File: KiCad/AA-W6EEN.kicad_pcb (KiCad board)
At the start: 2 copper layers, 90 x 44 mm, 68 parts, among them J1 ANT, J2 BATT-MODULE, J3 2.4" TFT with EC11, Q1 BF998, Q2 AO3401A, Q3 MMBT2222A, T1 Bifilar-10T, U1 Si5351A-B-GT, U2 LM358, U3 AMS1117-3.3

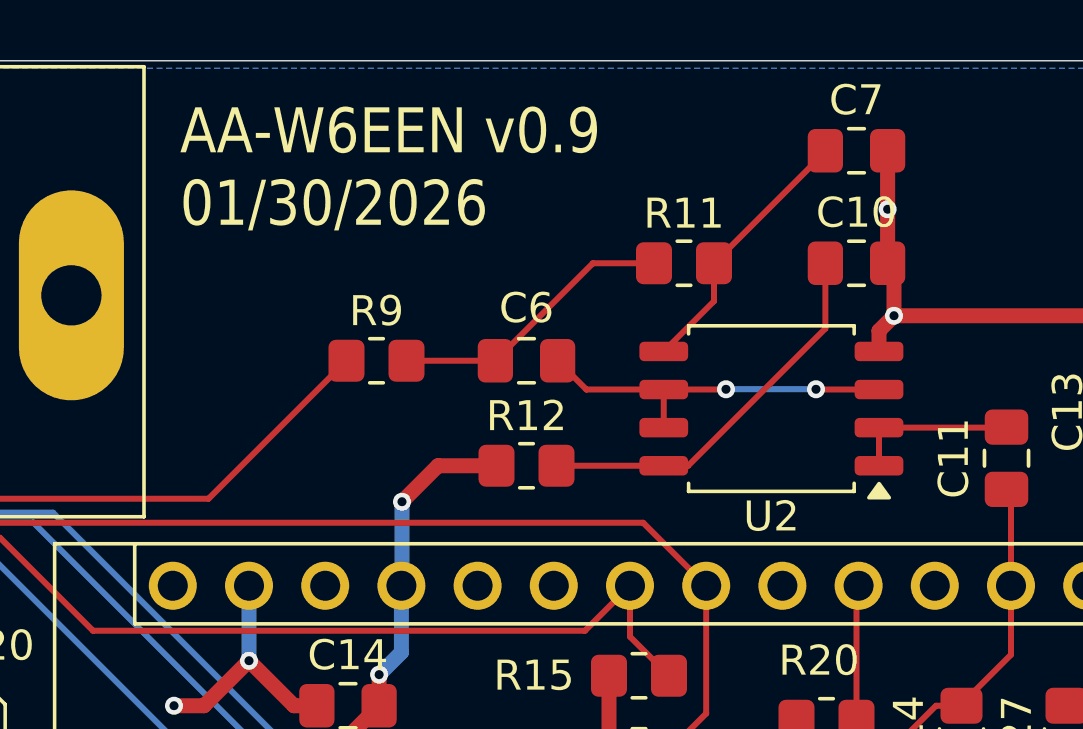
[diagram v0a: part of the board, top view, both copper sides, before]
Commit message: Updated OPAMP footprint. Changed date/revision.
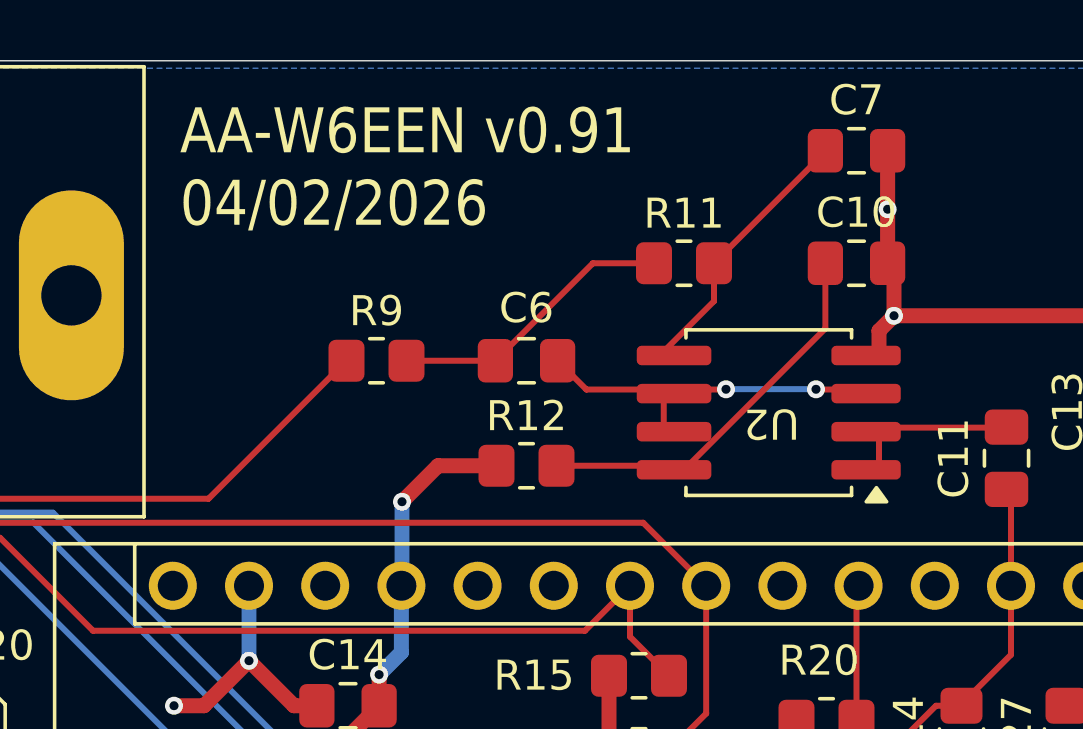
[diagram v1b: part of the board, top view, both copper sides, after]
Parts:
- U2: footprint Package_SO:SOIC-8_5.3x5.3mm_P1.27mm -> MY-SOIC8:My-SOIC8
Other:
- board text added: "AA-W6EEN v0.91 04/02/2026"
- board text removed: "AA-W6EEN v0.9 01/30/2026"
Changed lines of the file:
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@@
 		)
 	)
-	(footprint "Package_SO:SOIC-8_5.3x5.3mm_P1.27mm"
+	(footprint "MY-SOIC8:My-SOIC8"
 		(layer "F.Cu")
 		(at 100.4125 51.595 180)
-		(descr "SOIC, 8 Pin (JEITA/EIAJ ED-7311-19 variation 08-001-BBA and Atmel/Microchip, 208 mils width, https://www.jeita.or.jp/japanese/standard/book/ED-7311-19/#target/page_no=21, https://ww1.microchip.com/downloads/en/DeviceDoc/20005045C.pdf#page=23, https://ww1.microchip.com/downloads/en/DeviceDoc/doc2535.pdf#page=162), generated with kicad-footprint-generator ipc_gullwing_generator.py")
-		(tags "SOIC SO P-SOP SOP SOP-8 SO SO-8 8S2 S2AE/F K04-056 CASE-751BE SO8W 8-Pin-SOIC PSA W8-2 W8-4 W8MS-1 FPT-8P-M08")
 		(property "Reference" "U2"
-			(at 0 -3.6 0)
+			(at 0 -0.5 180)
+			(unlocked yes)
 			(layer "F.SilkS")
 			(effects
 				(font
 					(size 1 1)
-					(thickness 0.15)
+					(thickness 0.1)
 				)
 			)
 		)
 		(property "Value" "LM358"
-			(at 0 3.6 0)
+			(at 0 1 180)
+			(unlocked yes)
 			(layer "F.Fab")
 			(hide yes)
@@
 		)
 		(property "Datasheet" "http://www.ti.com/lit/ds/symlink/lm2904-n.pdf"
-			(at 0 0 0)
+			(at 0 0 180)
+			(unlocked yes)
 			(layer "F.Fab")
 			(hide yes)
 			(effects
 				(font
-					(size 1.27 1.27)
+					(size 1 1)
 					(thickness 0.15)
 				)
@@
 		)
 		(property "Description" "Low-Power, Dual Operational Amplifiers, DIP-8/SOIC-8/TO-99-8"
-			(at 0 0 0)
+			(at 0 0 180)
+			(unlocked yes)
 			(layer "F.Fab")
 			(hide yes)
 			(effects
 				(font
-					(size 1.27 1.27)
+					(size 1 1)
 					(thickness 0.15)
 				)
@@
 		(attr smd)
 		(fp_line
-			(start 2.76 2.76)
-			(end -2.76 2.76)
+			(start 2.8475 2.625)
+			(end -2.6725 2.625)
 			(stroke
 				(width 0.12)
@@
 		)
 		(fp_line
-			(start 2.76 2.49)
-			(end 2.76 2.76)
+			(start 2.8475 2.355)
+			(end 2.8475 2.625)
 			(stroke
 				(width 0.12)
@@
 		)
 		(fp_line
-			(start 2.76 -2.76)
-			(end 2.76 -2.49)
+			(start 2.8475 -2.895)
+			(end 2.8475 -2.625)
 			(stroke
 				(width 0.12)
@@
 		)
 		(fp_line
-			(start -2.76 2.76)
-			(end -2.76 2.49)
+			(start -2.6725 2.625)
+			(end -2.6725 2.355)
 			(stroke
 				(width 0.12)
@@
 		)
 		(fp_line
-			(start -2.76 -2.49)
-			(end -2.76 -2.76)
+			(start -2.6725 -2.625)
+			(end -2.6725 -2.895)
 			(stroke
 				(width 0.12)
@@
 		)
 		(fp_line
-			(start -2.76 -2.76)
-			(end 2.76 -2.76)
+			(start -2.6725 -2.895)
+			(end 2.8475 -2.895)
 			(stroke
 				(width 0.12)
@@
 		(fp_poly
 			(pts
-				(xy -3.59 -2.5) (xy -3.93 -2.97) (xy -3.25 -2.97)
+				(xy -3.5025 -2.635) (xy -3.8425 -3.105) (xy -3.1625 -3.105)
 			)
 			(stroke
@@
 		)
 		(fp_line
-			(start 4.65 2.48)
-			(end 2.9 2.48)
+			(start 4.7375 2.345)
+			(end 2.9875 2.345)
 			(stroke
 				(width 0.05)
@@
 		)
 		(fp_line
-			(start 4.65 -2.48)
-			(end 4.65 2.48)
+			(start 4.7375 -2.615)
+			(end 4.7375 2.345)
 			(stroke
 				(width 0.05)
@@
 		)
 		(fp_line
-			(start 2.9 2.9)
-			(end -2.9 2.9)
+			(start 2.9875 2.765)
+			(end -2.8125 2.765)
 			(stroke
 				(width 0.05)
@@
 		)
 		(fp_line
-			(start 2.9 2.48)
-			(end 2.9 2.9)
+			(start 2.9875 2.345)
+			(end 2.9875 2.765)
 			(stroke
 				(width 0.05)
@@
 		)
 		(fp_line
-			(start 2.9 -2.48)
-			(end 4.65 -2.48)
+			(start 2.9875 -2.615)
+			(end 4.7375 -2.615)
 			(stroke
 				(width 0.05)
@@
 		)
 		(fp_line
-			(start 2.9 -2.9)
-			(end 2.9 -2.48)
+			(start 2.9875 -3.035)
+			(end 2.9875 -2.615)
 			(stroke
 				(width 0.05)
@@
 		)
 		(fp_line
-			(start -2.9 2.9)
-			(end -2.9 2.48)
+			(start -2.8125 2.765)
+			(end -2.8125 2.345)
 			(stroke
 				(width 0.05)
@@
 		)
 		(fp_line
-			(start -2.9 2.48)
-			(end -4.65 2.48)
+			(start -2.8125 2.345)
+			(end -4.5625 2.345)
 			(stroke
 				(width 0.05)
@@
 		)
 		(fp_line
-			(start -2.9 -2.48)
-			(end -2.9 -2.9)
+			(start -2.8125 -2.615)
+			(end -2.8125 -3.035)
 			(stroke
 				(width 0.05)
@@
 		)
 		(fp_line
-			(start -2.9 -2.9)
-			(end 2.9 -2.9)
+			(start -2.8125 -3.035)
+			(end 2.9875 -3.035)
 			(stroke
 				(width 0.05)
@@
 		)
 		(fp_line
-			(start -4.65 2.48)
-			(end -4.65 -2.48)
+			(start -4.5625 2.345)
+			(end -4.5625 -2.615)
 			(stroke
 				(width 0.05)
@@
 		)
 		(fp_line
-			(start -4.65 -2.48)
-			(end -2.9 -2.48)
+			(start -4.5625 -2.615)
+			(end -2.8125 -2.615)
 			(stroke
 				(width 0.05)
@@
 		(fp_poly
 			(pts
-				(xy -1.65 -2.65) (xy 2.65 -2.65) (xy 2.65 2.65) (xy -2.65 2.65) (xy -2.65 -1.65)
+				(xy -2.5625 -1.785) (xy -2.5625 2.515) (xy 2.7375 2.515) (xy 2.7375 -2.785) (xy -1.5625 -2.785)
 			)
 			(stroke
@@
 			(layer "F.Fab")
 		)
+		(fp_text user "${REFERENCE}"
+			(at 0 2.5 180)
+			(unlocked yes)
+			(layer "F.Fab")
+			(effects
+				(font
+					(size 1 1)
+					(thickness 0.15)
+				)
+			)
+		)
 		(pad "1" smd roundrect
-			(at -3.5875 -1.905 180)
-			(size 1.625 0.65)
+			(at -3.15625 -2.04 180)
+			(size 2.3125 0.65)
 			(layers "F.Cu" "F.Mask" "F.Paste")
 			(roundrect_rratio 0.25)
@@
 		)
 		(pad "2" smd roundrect
-			(at -3.5875 -0.635 180)
-			(size 1.625 0.65)
+			(at -3.15625 -0.77 180)
+			(size 2.3125 0.65)
 			(layers "F.Cu" "F.Mask" "F.Paste")
 			(roundrect_rratio 0.25)
@@
 		)
 		(pad "3" smd roundrect
-			(at -3.5875 0.635 180)
-			(size 1.625 0.65)
+			(at -3.15625 0.5 180)
+			(size 2.3125 0.65)
 			(layers "F.Cu" "F.Mask" "F.Paste")
 			(roundrect_rratio 0.25)
@@
 		)
 		(pad "4" smd roundrect
-			(at -3.5875 1.905 180)
-			(size 1.625 0.65)
+			(at -3.15625 1.77 180)
+			(size 2.3125 0.65)
 			(layers "F.Cu" "F.Mask" "F.Paste")
 			(roundrect_rratio 0.25)
@@
 		)
 		(pad "5" smd roundrect
-			(at 3.5875 1.905 180)
-			(size 1.625 0.65)
+			(at 3.24375 1.77 180)
+			(size 2.4875 0.65)
 			(layers "F.Cu" "F.Mask" "F.Paste")
 			(roundrect_rratio 0.25)
@@
 		)
 		(pad "6" smd roundrect
-			(at 3.5875 0.635 180)
-			(size 1.625 0.65)
+			(at 3.24375 0.5 180)
+			(size 2.4875 0.65)
 			(layers "F.Cu" "F.Mask" "F.Paste")
 			(roundrect_rratio 0.25)
@@
 		)
 		(pad "7" smd roundrect
-			(at 3.5875 -0.635 180)
-			(size 1.625 0.65)
+			(at 3.24375 -0.77 180)
+			(size 2.4875 0.65)
 			(layers "F.Cu" "F.Mask" "F.Paste")
 			(roundrect_rratio 0.25)
@@
 		)
 		(pad "8" smd roundrect
-			(at 3.5875 -1.905 180)
-			(size 1.625 0.65)
+			(at 3.24375 -2.04 180)
+			(size 2.4875 0.65)
 			(layers "F.Cu" "F.Mask" "F.Paste")
 			(roundrect_rratio 0.25)
@@
 		)
 		(embedded_fonts no)
-		(model "${KICAD9_3DMODEL_DIR}/Package_SO.3dshapes/SOIC-8_5.3x5.3mm_P1.27mm.step"
-			(offset
-				(xyz 0 0 0)
-			)
-			(scale
-				(xyz 1 1 1)
-			)
-			(rotate
-				(xyz 0 0 0)
-			)
-		)
 	)
 	(footprint "Capacitor_SMD:C_0805_2012Metric_Pad1.18x1.45mm_HandSolder"
@@
 		(layer "Edge.Cuts")
 	)
-	(gr_text "AA-W6EEN v0.9\n01/30/2026"
+	(gr_text "AA-W6EEN v0.91\n04/02/2026"
 		(at 80.7 45.65 0)
 		(layer "F.SilkS")
@@
 	)
 	(gr_text "STEP-IN"
-		(at 67 78.45 270)
+		(at 64.2 78.5 270)
 		(layer "B.SilkS")
 		(effects
@@
 	)
 	(gr_text "CHRG-OUT"
-		(at 64.2 78.5 270)
+		(at 67 78.45 270)
 		(layer "B.SilkS")
 		(effects
